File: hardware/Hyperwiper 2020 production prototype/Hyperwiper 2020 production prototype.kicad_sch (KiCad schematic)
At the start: 20 parts, among them J1 Conn_01x05, K1 Main Power relay, K2 Wiper control relay, Q1 PN2222A, SW1 ON-OFF, SW2 SW_Reed, U1 Teensy4.0, U3 L7805

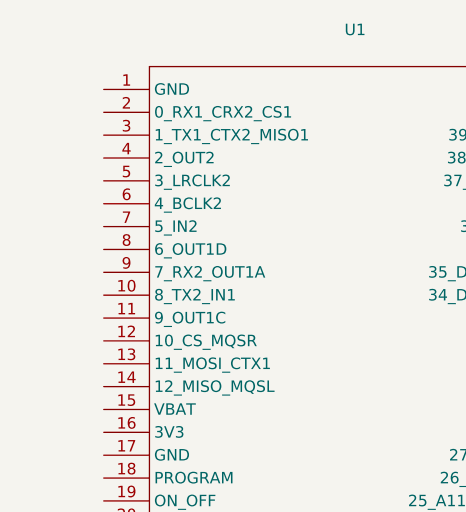
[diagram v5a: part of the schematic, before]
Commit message: Adde routing for the RGB leds
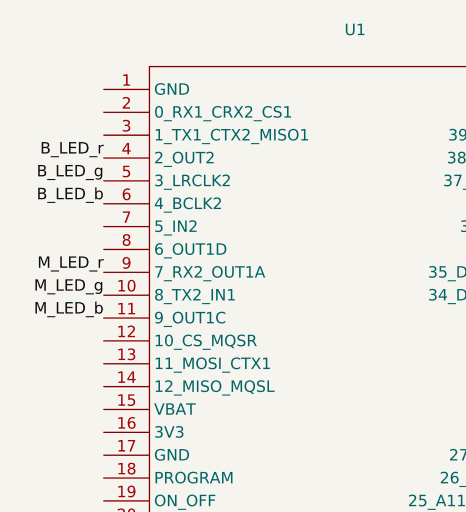
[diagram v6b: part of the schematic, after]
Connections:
- net B_LED_b: now also U1.6 (4_BCLK2)
- net B_LED_g: now also U1.5 (3_LRCLK2)
- net B_LED_r: now also U1.4 (2_OUT2)
- net M_LED_b: now also U1.11 (9_OUT1C)
- net M_LED_g: now also U1.10 (8_TX2_IN1)
- net M_LED_r: now also U1.9 (7_RX2_OUT1A)
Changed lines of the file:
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@@
     (effects (font (size 2.5 2.5)) (justify right bottom))
+  )
+  (label "B_LED_r" (at 52.07 33.02 180)
+    (effects (font (size 1.27 1.27)) (justify right bottom))
+  )
+  (label "B_LED_g" (at 52.07 35.56 180)
+    (effects (font (size 1.27 1.27)) (justify right bottom))
+  )
+  (label "B_LED_b" (at 52.07 38.1 180)
+    (effects (font (size 1.27 1.27)) (justify right bottom))
+  )
+  (label "M_LED_r" (at 52.07 45.72 180)
+    (effects (font (size 1.27 1.27)) (justify right bottom))
+  )
+  (label "M_LED_g" (at 52.07 48.26 180)
+    (effects (font (size 1.27 1.27)) (justify right bottom))
+  )
+  (label "M_LED_b" (at 52.07 50.8 180)
+    (effects (font (size 1.27 1.27)) (justify right bottom))
   )
   (label "M_LED_b" (at 153.67 111.76 180)

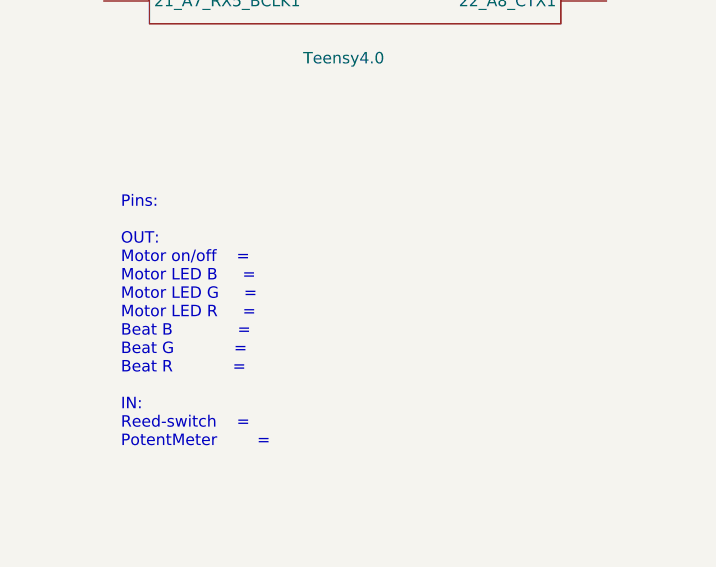
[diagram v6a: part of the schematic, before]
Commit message: Updated pin numbers
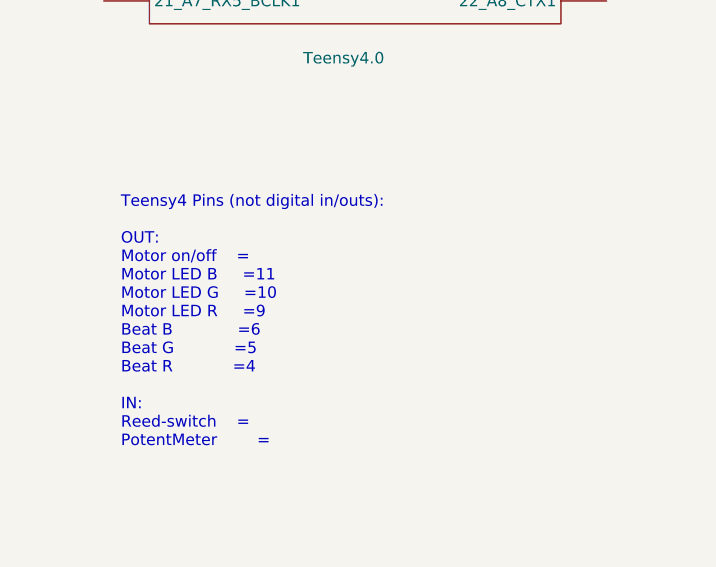
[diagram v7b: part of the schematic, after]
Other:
- note added: "Teensy4 Pins (not digital in/outs): OUT: Motor on/off = Motor LED B =11 Motor LED G =10 Motor LED R =9 Beat B =6 Beat G =5 Beat R =4 IN: Reed-switch = PotentMeter ="
- note removed: "Pins: OUT: Motor on/off = Motor LED B = Motor LED G = Motor LED R = Beat B = Beat G = Beat R = IN: Reed-switch = PotentMeter ="
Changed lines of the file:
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@@
     (stroke (width 0) (type solid) (color 0 0 0 0))
   )
-  (text "Pins:\n\nOUT:\nMotor on/off	=\nMotor LED B 	=\nMotor LED G 	=\nMotor LED R 	=\nBeat B 			=\nBeat G			=\nBeat R			=\n\nIN:\nReed-switch	=\nPotentMeter		=\n\n\n\n"
+  (text "Teensy4 Pins (not digital in/outs):\n\nOUT:\nMotor on/off	=\nMotor LED B 	=11\nMotor LED G 	=10\nMotor LED R 	=9\nBeat B 			=6\nBeat G			=5\nBeat R			=4\n\nIN:\nReed-switch	=\nPotentMeter		=\n\n\n\n"
     (at 53.975 149.86 0)
     (effects (font (size 1.27 1.27)) (justify left bottom))

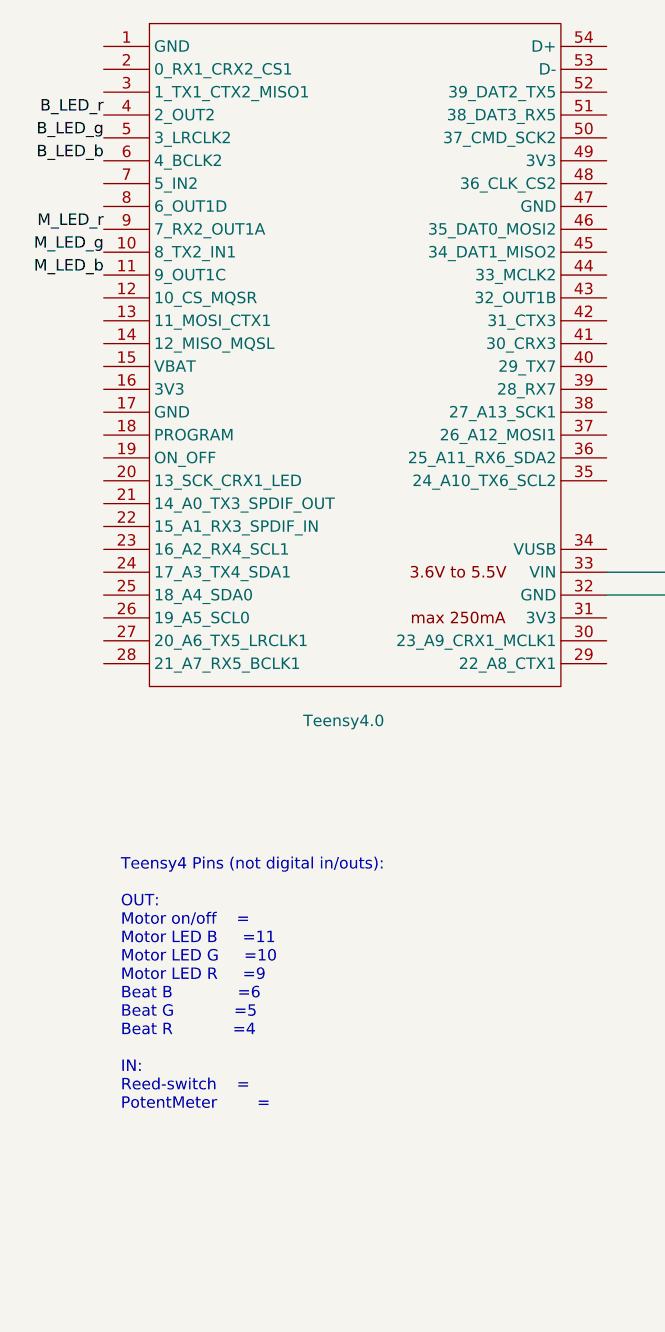
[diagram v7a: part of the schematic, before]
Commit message: Added flowchart drafts and modified pin number after finding conflics with the audio board I2C bus
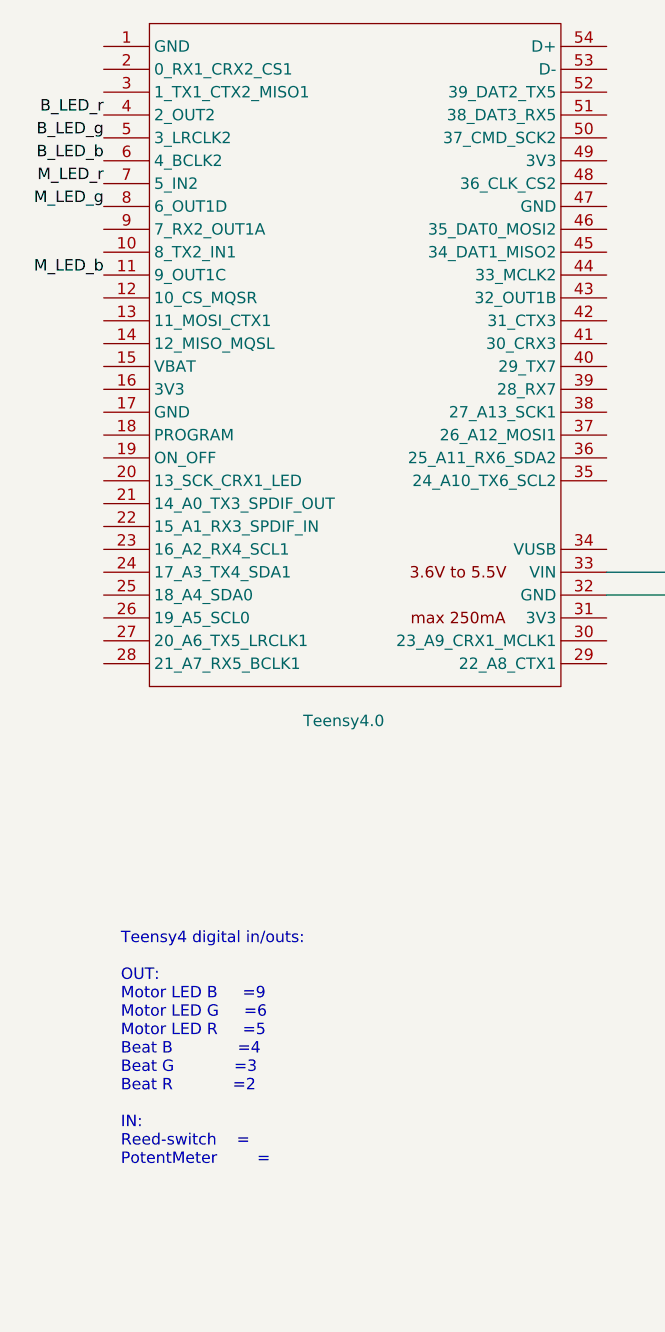
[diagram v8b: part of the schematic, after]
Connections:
- net M_LED_g: now also U1.8 (6_OUT1D); no longer U1.10 (8_TX2_IN1)
- net M_LED_r: now also U1.7 (5_IN2); no longer U1.9 (7_RX2_OUT1A)
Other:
- note added: "Teensy4 digital in/outs: OUT: Motor LED B =9 Motor LED G =6 Motor LED R =5 Beat B =4 Beat G =3 Beat R =2 IN: Reed-switch = PotentMeter ="
- note removed: "Teensy4 Pins (not digital in/outs): OUT: Motor on/off = Motor LED B =11 Motor LED G =10 Motor LED R =9 Beat B =6 Beat G =5 Beat R =4 IN: Reed-switch = PotentMeter ="
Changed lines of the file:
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@@
     (stroke (width 0) (type solid) (color 0 0 0 0))
   )
-  (text "Teensy4 Pins (not digital in/outs):\n\nOUT:\nMotor on/off	=\nMotor LED B 	=11\nMotor LED G 	=10\nMotor LED R 	=9\nBeat B 			=6\nBeat G			=5\nBeat R			=4\n\nIN:\nReed-switch	=\nPotentMeter		=\n\n\n\n"
+  (text "Teensy4 digital in/outs:\n\nOUT:\nMotor LED B 	=9\nMotor LED G 	=6\nMotor LED R 	=5\nBeat B 			=4\nBeat G			=3\nBeat R			=2\n\nIN:\nReed-switch	=\nPotentMeter		="
     (at 53.975 149.86 0)
     (effects (font (size 1.27 1.27)) (justify left bottom))
@@
     (effects (font (size 1.27 1.27)) (justify right bottom))
   )
-  (label "M_LED_r" (at 52.07 45.72 180)
+  (label "M_LED_r" (at 52.07 40.64 180)
     (effects (font (size 1.27 1.27)) (justify right bottom))
   )
-  (label "M_LED_g" (at 52.07 48.26 180)
+  (label "M_LED_g" (at 52.07 43.18 180)
     (effects (font (size 1.27 1.27)) (justify right bottom))
   )
